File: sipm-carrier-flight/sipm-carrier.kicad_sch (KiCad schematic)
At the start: 20 parts, among them J1 Conn_Coaxial_Small, J2 output, J3 Conn_02x02_Top_Bottom

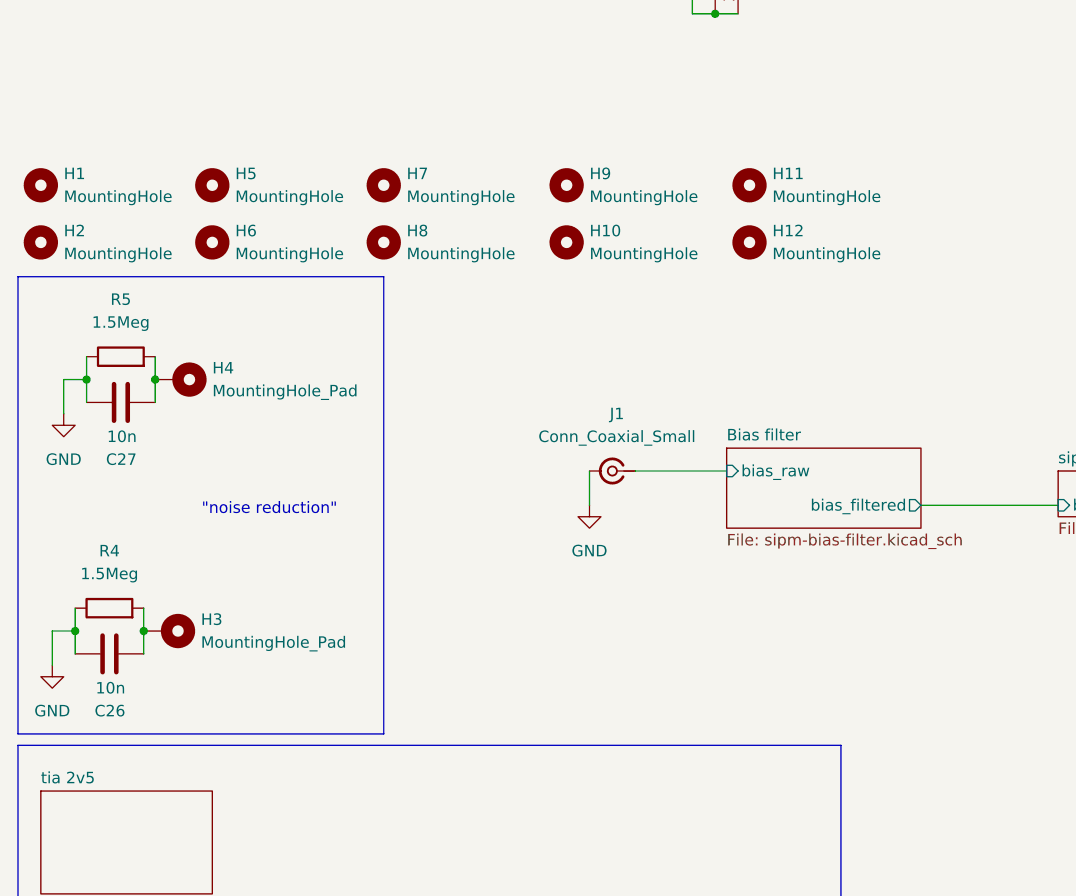
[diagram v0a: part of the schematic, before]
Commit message: updated per MSU comments
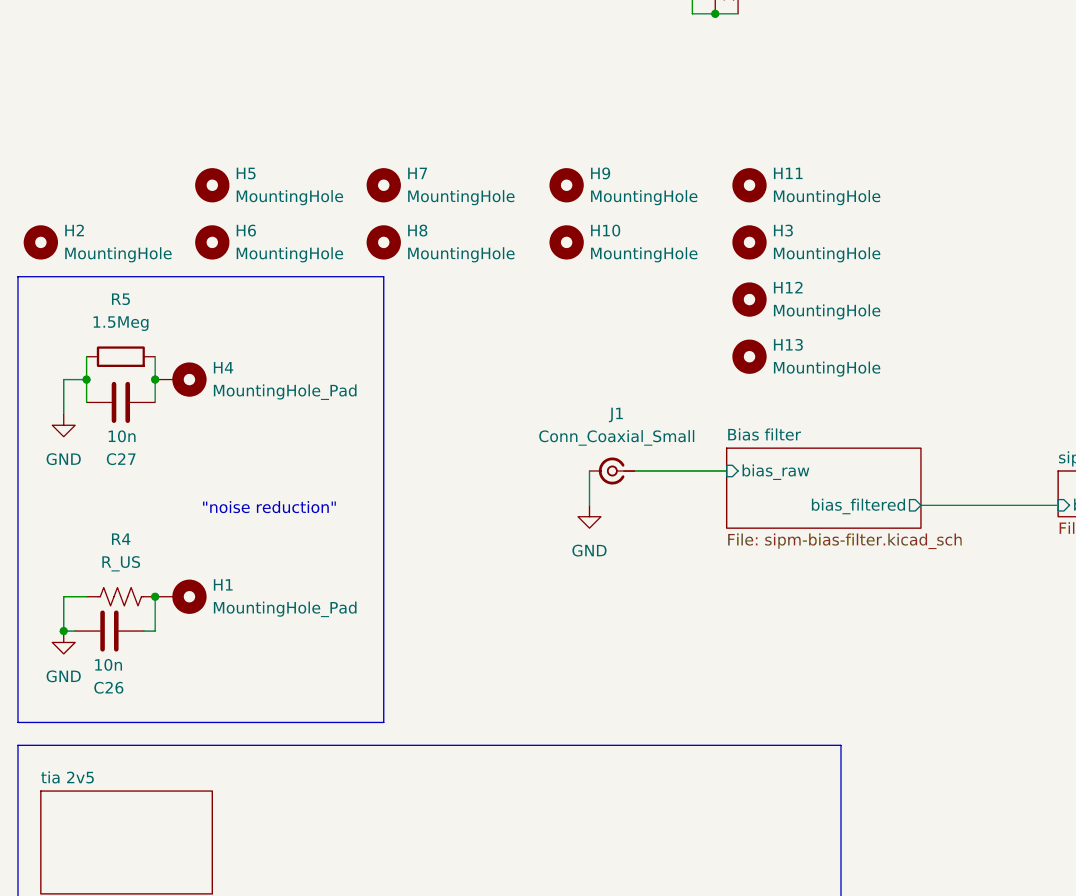
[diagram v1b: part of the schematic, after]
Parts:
- removed H1: MountingHole, MountingHole:MountingHole_3.2mm_M3, symbol Mechanical:MountingHole
- removed H3: MountingHole_Pad, MountingHole:MountingHole_3.2mm_M3_DIN965_Pad, symbol Mechanical:MountingHole_Pad
- removed R4: 1.5Meg, Resistor_SMD:R_1206_3216Metric_Pad1.30x1.75mm_HandSolder, symbol Device:R
- added H1: MountingHole_Pad, MountingHole:MountingHole_3.2mm_M3_DIN965_Pad, symbol Mechanical:MountingHole_Pad
- added H13, H3: MountingHole, MountingHole:MountingHole_3.2mm_M3, symbol Mechanical:MountingHole
- added R4: R_US, Resistor_SMD:R_0805_2012Metric_Pad1.20x1.40mm_HandSolder, symbol Device:R_US
- C26: footprint Capacitor_SMD:C_1206_3216Metric_Pad1.33x1.80mm_HandSolder -> Capacitor_SMD:C_0805_2012Metric_Pad1.18x1.45mm_HandSolder
- J2: footprint Library:TE_CONSMA020.062-G -> Connector_Coaxial:MMCX_Molex_73415-0961_Horizontal_1.6mm-PCB
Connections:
- net GND: now also C26.2, R4.1; no longer C26.1
- new net: C26.1, H1.1, R4.2

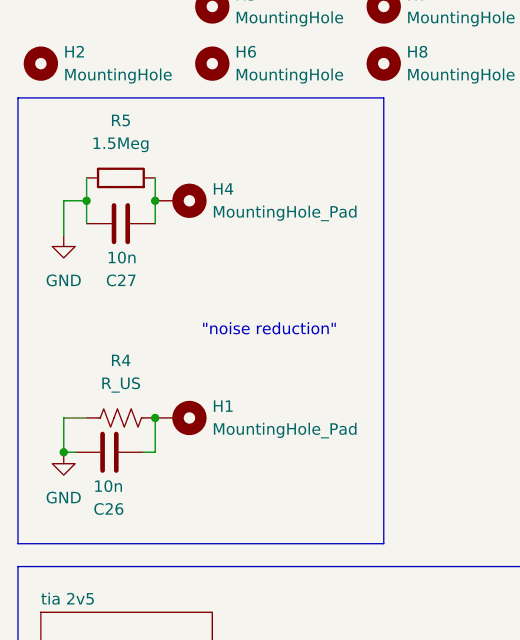
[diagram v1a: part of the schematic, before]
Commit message: sipm board pre-production
- verify spcaing between SiPMs
- move silkscreens around so that they are not overlapping
- change footprints to be hand-solder type in case someone has to do that
- change values of some components to unify part list (e.g. any 100n are now 0.1u)
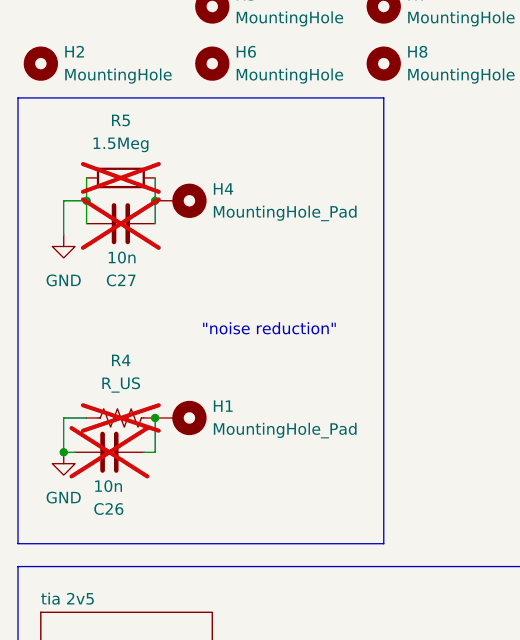
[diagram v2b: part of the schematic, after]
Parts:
- C26, C27, R4, R5: now not fitted; now left out of the parts list
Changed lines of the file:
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@@
 		(unit 1)
 		(exclude_from_sim no)
-		(in_bom yes)
-		(on_board yes)
-		(dnp no)
+		(in_bom no)
+		(on_board yes)
+		(dnp yes)
 		(property "Reference" "C26"
 			(at 22.352 152.4 90)
@@
 		(unit 1)
 		(exclude_from_sim no)
-		(in_bom yes)
-		(on_board yes)
-		(dnp no)
+		(in_bom no)
+		(on_board yes)
+		(dnp yes)
 		(property "Reference" "R4"
 			(at 25.4 135.89 90)
@@
 		(unit 1)
 		(exclude_from_sim no)
-		(in_bom yes)
-		(on_board yes)
-		(dnp no)
+		(in_bom no)
+		(on_board yes)
+		(dnp yes)
 		(property "Reference" "C27"
 			(at 27.178 127 90)
@@
 		(unit 1)
 		(exclude_from_sim no)
-		(in_bom yes)
-		(on_board yes)
-		(dnp no)
+		(in_bom no)
+		(on_board yes)
+		(dnp yes)
 		(fields_autoplaced yes)
 		(property "Reference" "R5"
